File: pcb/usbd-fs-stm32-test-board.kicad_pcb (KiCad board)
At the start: 2 copper layers, 85.1 x 56 mm, 28 parts, among them J1 USB_B_Mini, J2 USB_B_Mini, U1 USBLC6-2SC6, U2 USBLC6-2SC6

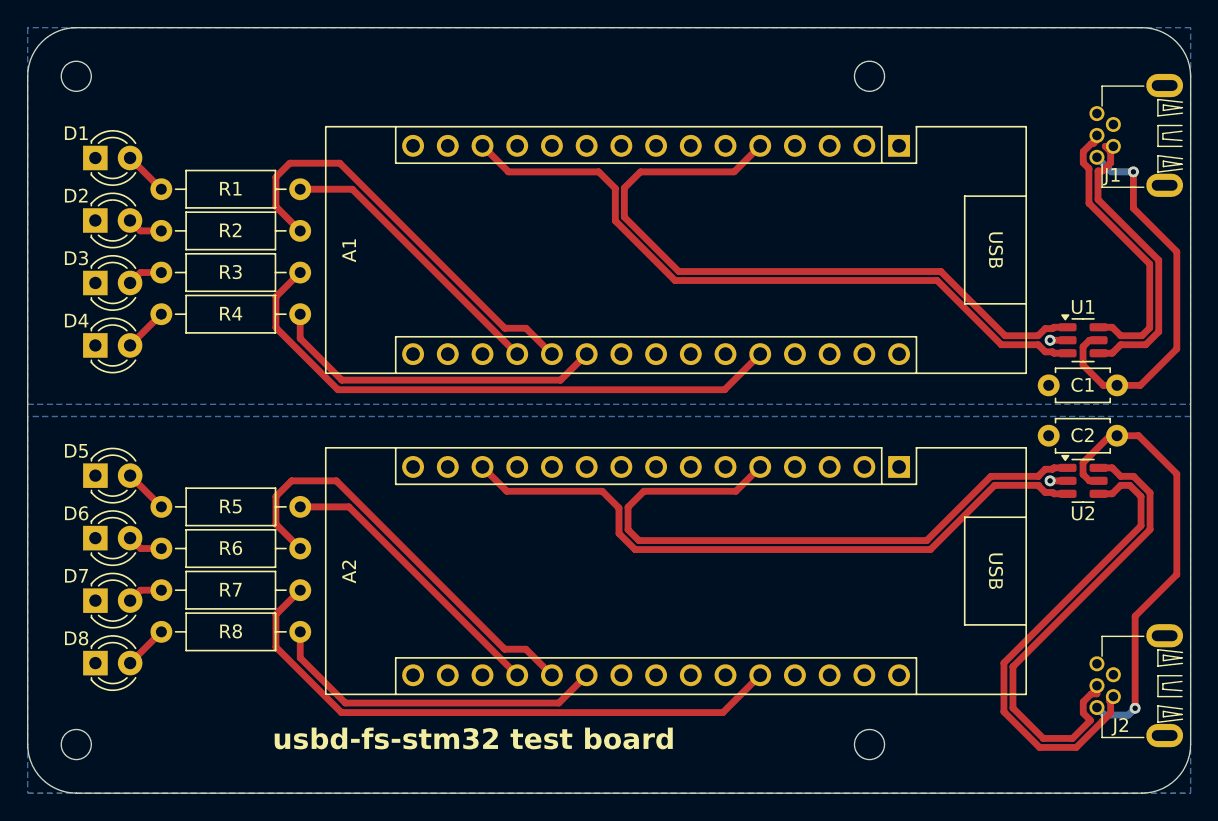
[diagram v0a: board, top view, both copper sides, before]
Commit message: pcb: revision 20241120: fixed conflict of LED pins with VCP pins
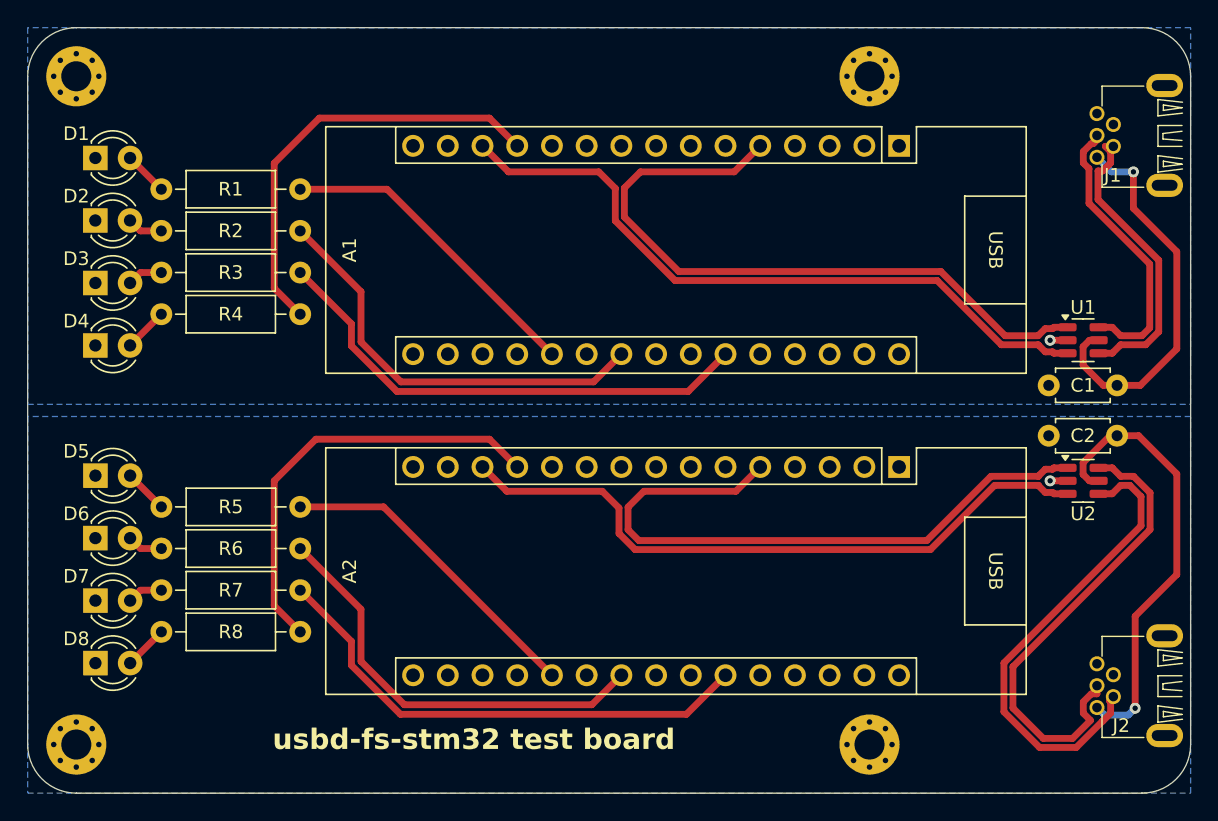
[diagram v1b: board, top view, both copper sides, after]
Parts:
- H1, H2, H3, H4: footprint MountingHole:MountingHole_2.2mm_M2 -> MountingHole:MountingHole_2.2mm_M2_Pad_Via
- moved H2 75.9 mm to (151.1, 82.4)
- moved H3 75.9 mm to (93.1, 131.3)
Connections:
- A1 pad 12: unconnected-(A1-D9-Pad12) -> D4
- A1 pad 19: Net-(A1-A0) -> unconnected-(A1-A0-Pad19)
- A1 pad 20: Net-(A1-A1) -> D1
- A1 pad 21: Net-(A1-A2) -> unconnected-(A1-A2-Pad21)
- A1 pad 22: unconnected-(A1-A3-Pad22) -> D2
- A1 pad 25: unconnected-(A1-A6-Pad25) -> D3
- A1 pad 26: Net-(A1-A7) -> unconnected-(A1-A7-Pad26)
- A2 pad 12: unconnected-(A2-D9-Pad12) -> D8
- A2 pad 19: Net-(A2-A0) -> unconnected-(A2-A0-Pad19)
- A2 pad 20: Net-(A2-A1) -> D5
- A2 pad 21: Net-(A2-A2) -> unconnected-(A2-A2-Pad21)
- A2 pad 22: unconnected-(A2-A3-Pad22) -> D6
- A2 pad 25: unconnected-(A2-A6-Pad25) -> D7
- A2 pad 26: Net-(A2-A7) -> unconnected-(A2-A7-Pad26)
- R1 pad 1: Net-(A1-A0) -> D1
- R2 pad 1: Net-(A1-A1) -> D2
- R3 pad 1: Net-(A1-A7) -> D3
- R4 pad 1: Net-(A1-A2) -> D4
- R5 pad 1: Net-(A2-A0) -> D5
- R6 pad 1: Net-(A2-A1) -> D6
- R7 pad 1: Net-(A2-A7) -> D7
- R8 pad 1: Net-(A2-A2) -> D8
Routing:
- net Net-(A2-A7): track 43.5 -> 0.00 mm
- net Net-(A1-A7): track 43.2 -> 0.00 mm
- net D7: track 0.00 -> 37.1 mm
- net D3: track 0.00 -> 36.8 mm
- net D4: track 0.00 -> 31.8 mm
- net D8: track 0.00 -> 31.7 mm
- net D6: track 0.00 -> 31.4 mm
- net Net-(A2-A1): track 31.1 -> 0.00 mm
- net D2: track 0.00 -> 31.1 mm
- net Net-(A1-A1): track 31.1 -> 0.00 mm
- net Net-(A2-A2): track 25.1 -> 0.00 mm
- net Net-(A1-A2): track 24.8 -> 0.00 mm
- net D5: track 0.00 -> 23.5 mm
- net D1: track 0.00 -> 23.4 mm
- net Net-(A2-A0): track 21.0 -> 0.00 mm
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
